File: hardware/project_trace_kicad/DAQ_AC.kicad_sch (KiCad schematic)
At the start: 1 part, among them U301 ADC3542

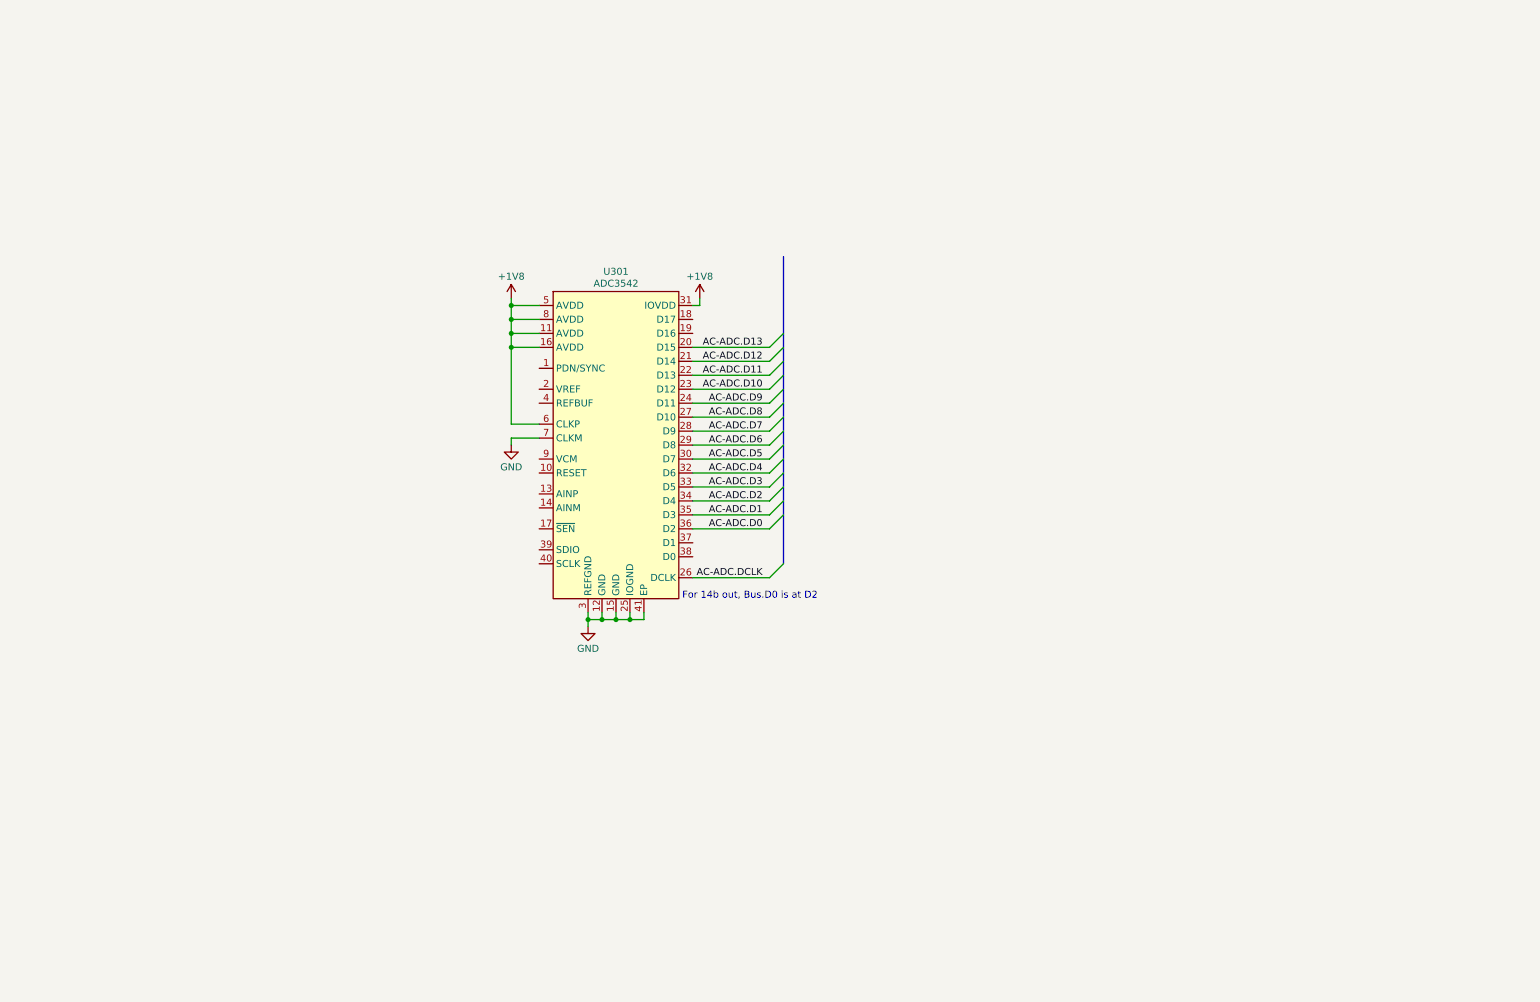
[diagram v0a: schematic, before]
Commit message: Added DAQ_AC and DAC
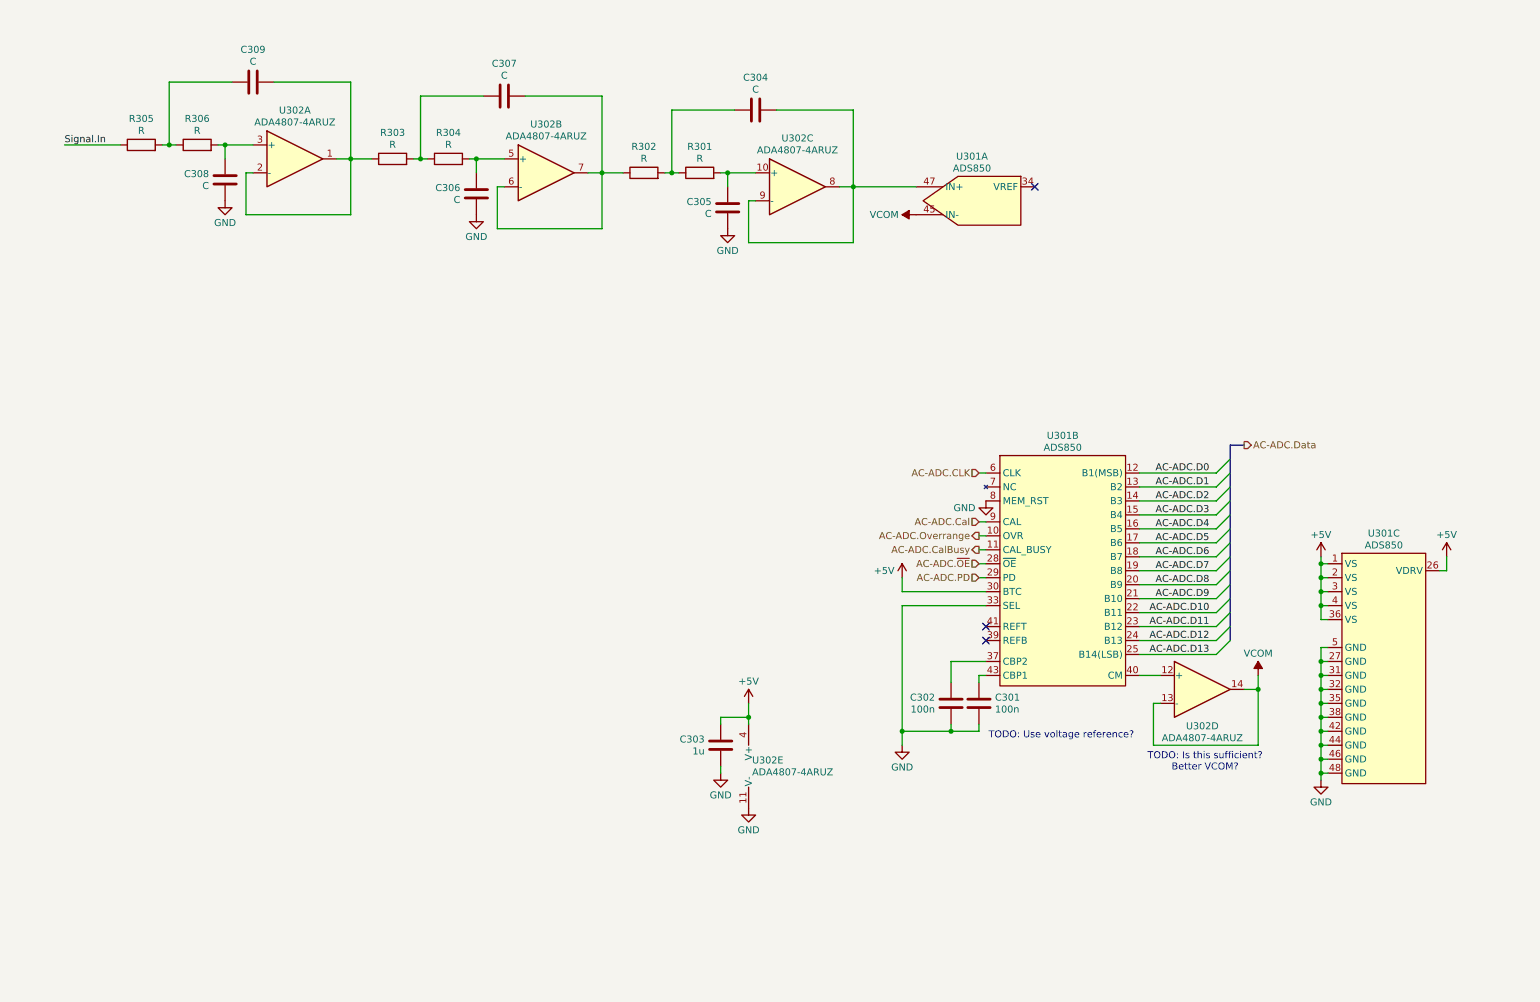
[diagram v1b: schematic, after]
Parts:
- removed U301: ADC3542, ProjectTraceFootprints:QFN-40_EP_5.1x5.1_Pitch0.4mm-RSB0040F, symbol ProjectTraceSymbols:ADC3542
- added C301, C302: 100n, symbol Device:C
- added C303: 1u, symbol Device:C
- added C304, C305, C306, C307, C308, C309: C, symbol Device:C
- added R301, R302, R303, R304, R305, R306: R, symbol Device:R
- added U301: ADS850, Package_QFP:TQFP-48_7x7mm_P0.5mm, symbol ProjectTraceSymbols:ADS850
- added U302: ADA4807-4ARUZ, Package_SO:TSSOP-14_4.4x5mm_P0.65mm, symbol Amplifier_Operational:ADA4807-4ARUZ
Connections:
- net AC-ADC.D0: now also U301.12 (B1(MSB))
- net AC-ADC.D1: now also U301.13 (B2)
- net AC-ADC.D10: now also U301.22 (B11)
- net AC-ADC.D11: now also U301.23 (B12)
- net AC-ADC.D12: now also U301.24 (B13)
- net AC-ADC.D13: now also U301.25 (B14(LSB))
- net AC-ADC.D2: now also U301.14 (B3)
- net AC-ADC.D3: now also U301.15 (B4)
- net AC-ADC.D4: now also U301.16 (B5)
- net AC-ADC.D5: now also U301.17 (B6)
- net AC-ADC.D6: now also U301.18 (B7)
- net AC-ADC.D7: now also U301.19 (B8)
- net AC-ADC.D8: now also U301.20 (B9)
- net AC-ADC.D9: now also U301.21 (B10)
- net GND: now also C301.2, C302.2, C303.1, C305.1, C306.1, C308.1, U301.27 (GND), U301.31 (GND), U301.32 (GND), U301.33 (SEL), U301.35 (GND), U301.38 (GND), U301.42 (GND), U301.44 (GND), U301.46 (GND), U301.48 (GND), U301.5 (GND), U301.8 (MEM_RST), U302.11 (V-)
- new net: C306.2, R304.2, U302.5 (+)
- new net: C307.2, R302.1, U302.6 (-), U302.7
- new net: C309.2, R303.1, U302.1, U302.2 (-)
- new net: C307.1, R303.2, R304.1
- new net: C305.2, R301.2, U302.10 (+)
- new net: C304.2, U301.47 (IN+), U302.8, U302.9 (-)
- new net: C304.1, R301.1, R302.2
- new net: C301.1, U301.43 (CBP1)
- new net: U301.40 (CM), U302.12 (+)
- new net: C302.1, U301.37 (CBP2)
- new net: C309.1, R305.2, R306.1
- new net: C308.2, R306.2, U302.3 (+)
- new net +5V: C303.2, U301.1 (VS), U301.2 (VS), U301.26 (VDRV), U301.3 (VS), U301.30 (BTC), U301.36 (VS), U301.4 (VS), U302.4 (V+)
- new net AC-ADC.CLK: U301.6 (CLK)
- new net AC-ADC.Cal: U301.9 (CAL)
- new net AC-ADC.CalBusy: U301.11 (CAL_BUSY)
- new net AC-ADC.Overrange: U301.10 (OVR)
- new net AC-ADC.PD: U301.29 (PD)
- new net AC-ADC.~{OE}: U301.28 (~{OE})
- new net Signal.In: R305.1
- new net VCOM: U301.45 (IN-), U302.13 (-), U302.14
- no-connect marks 0 -> 3
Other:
- note added: "TODO: Is this sufficient? Better VCOM?"
- note added: "TODO: Use voltage reference?"
- note removed: "For 14b out, Bus.D0 is at D2"

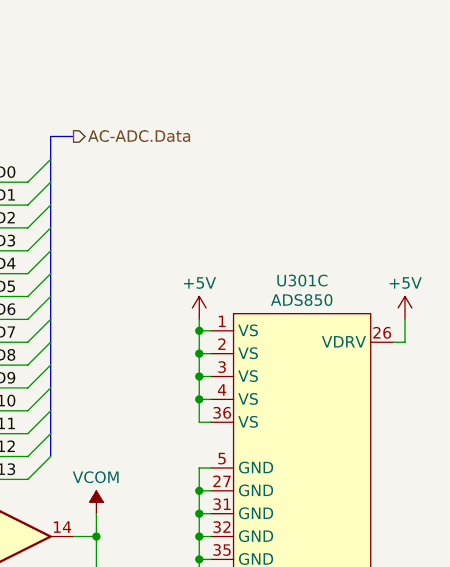
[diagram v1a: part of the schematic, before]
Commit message: Changes to DAQ-AC and Inputs
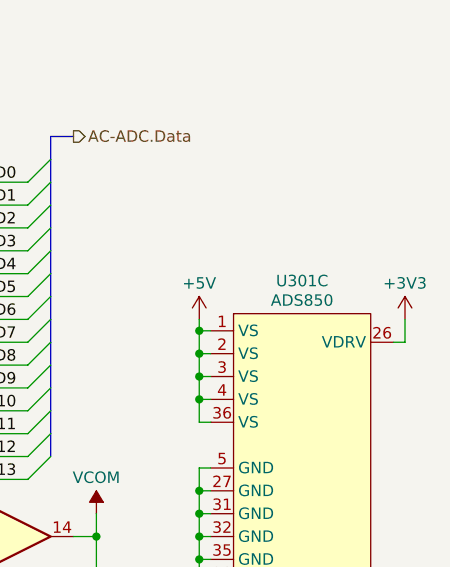
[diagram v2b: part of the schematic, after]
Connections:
- net +5V: no longer U301.26 (VDRV)
- new net +3V3: U301.26 (VDRV)
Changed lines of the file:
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@@
+	)
+	(symbol
+		(lib_id "power:+3V3")
+		(at 270.51 118.11 0)
+		(unit 1)
+		(exclude_from_sim no)
+		(in_bom yes)
+		(on_board yes)
+		(dnp no)
+		(fields_autoplaced yes)
+		(property "Reference" "#PWR0304"
+			(at 270.51 121.92 0)
+			(effects
+				(font
+					(size 1.27 1.27)
+				)
+				(hide yes)
+			)
+		)
+		(property "Value" "+3V3"
+			(at 270.51 114.1052 0)
+			(effects
+				(font
+					(size 1.27 1.27)
+				)
+			)
+		)
+		(property "Footprint" ""
+			(at 270.51 118.11 0)
+			(effects
+				(font
+					(size 1.27 1.27)
+				)
+				(hide yes)
+			)
+		)
+		(property "Datasheet" ""
+			(at 270.51 118.11 0)
+			(effects
+				(font
+					(size 1.27 1.27)
+				)
+				(hide yes)
+			)
+		)
+		(property "Description" "Power symbol creates a global label with name \"+3V3\""
+			(at 270.51 118.11 0)
+			(effects
+				(font
+					(size 1.27 1.27)
+				)
+				(hide yes)
+			)
+		)
+		(pin "1"
+		)
+		(instances
+			(project ""
+				(path "/af51f4e5-b952-4b0e-baf2-78a72fb86fcd/ac2add4a-2a5e-456c-897d-914b794115d5"
+					(reference "#PWR0304")
+					(unit 1)
+				)
+			)
+		)
 	)
 	(symbol
@@
 					(unit 1)
 				)
-			)
-		)
-	)
-	(symbol
-		(lib_id "power:+5V")
-		(at 270.51 118.11 0)
-		(unit 1)
-		(exclude_from_sim no)
-		(in_bom yes)
-		(on_board yes)
-		(dnp no)
-		(fields_autoplaced yes)
-		(property "Reference" "#PWR0304"
-			(at 270.51 121.92 0)
-			(effects
-				(font
-					(size 1.27 1.27)
-				)
-				(hide yes)
-			)
-		)
-		(property "Value" "+5V"
-			(at 270.51 114.1052 0)
-			(effects
-				(font
-					(size 1.27 1.27)
-				)
-			)
-		)
-		(property "Footprint" ""
-			(at 270.51 118.11 0)
-			(effects
-				(font
-					(size 1.27 1.27)
-				)
-				(hide yes)
-			)
-		)
-		(property "Datasheet" ""
-			(at 270.51 118.11 0)
-			(effects
-				(font
-					(size 1.27 1.27)
-				)
-				(hide yes)
-			)
-		)
-		(property "Description" "Power symbol creates a global label with name \"+5V\""
-			(at 270.51 118.11 0)
-			(effects
-				(font
-					(size 1.27 1.27)
-				)
-				(hide yes)
-			)
-		)
-		(pin "1"
-		)
-		(instances
-			(project "project_trace_kicad"
-				(path "/af51f4e5-b952-4b0e-baf2-78a72fb86fcd/ac2add4a-2a5e-456c-897d-914b794115d5"
-					(reference "#PWR0304")
-					(unit 1)
-				)

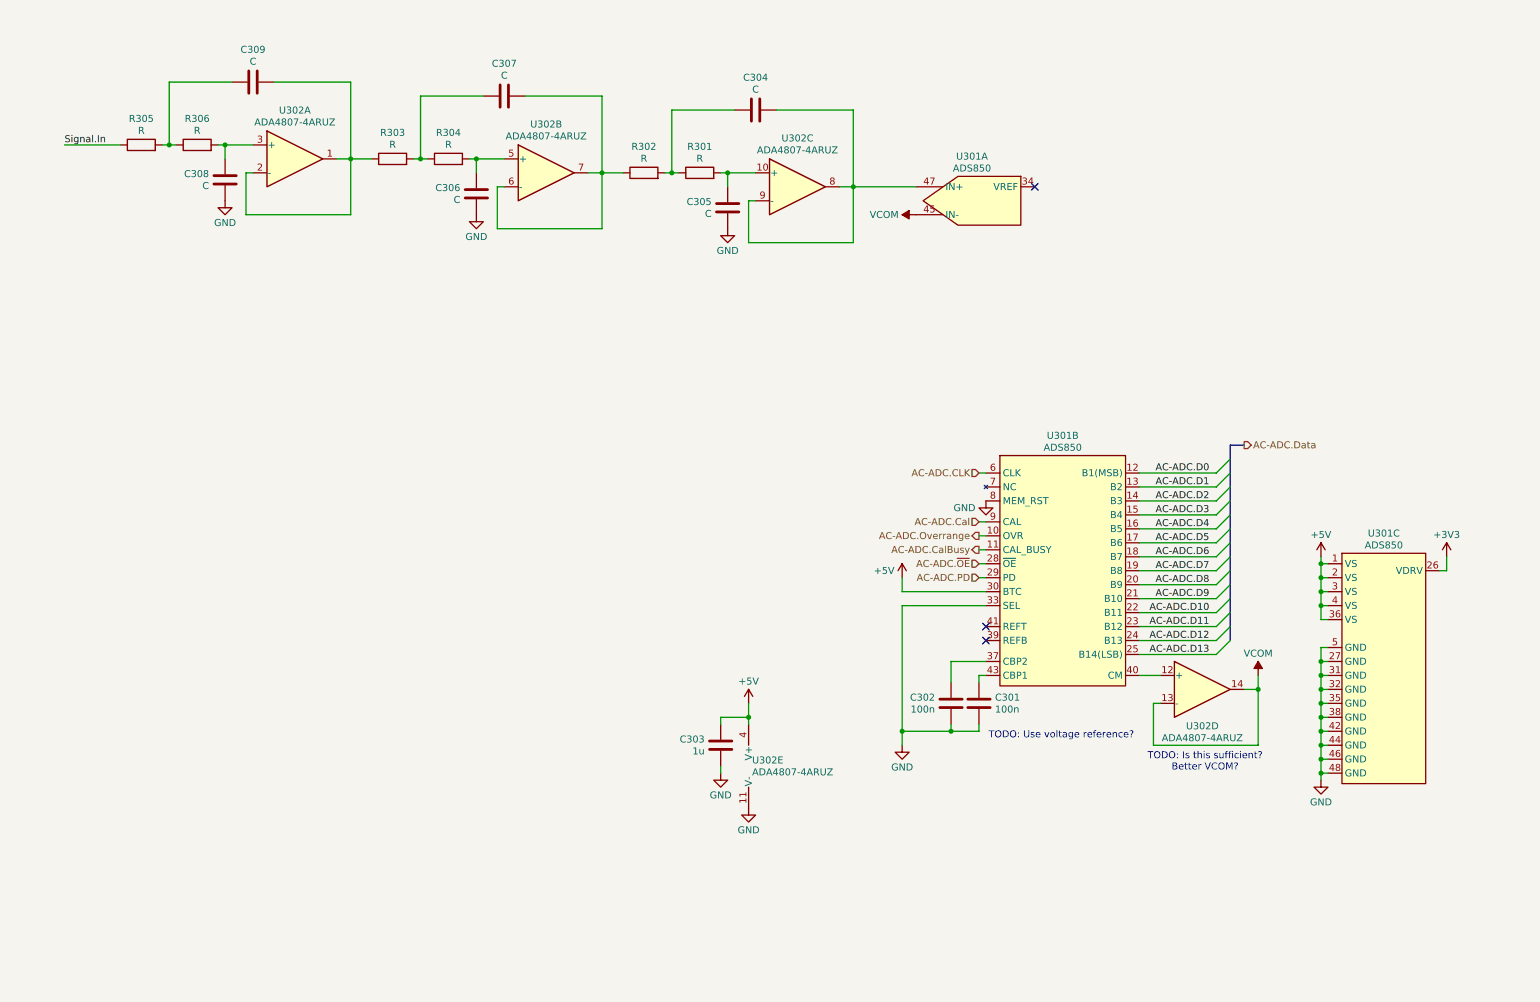
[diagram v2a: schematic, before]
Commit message: Add Decoupling, Fix Bugs
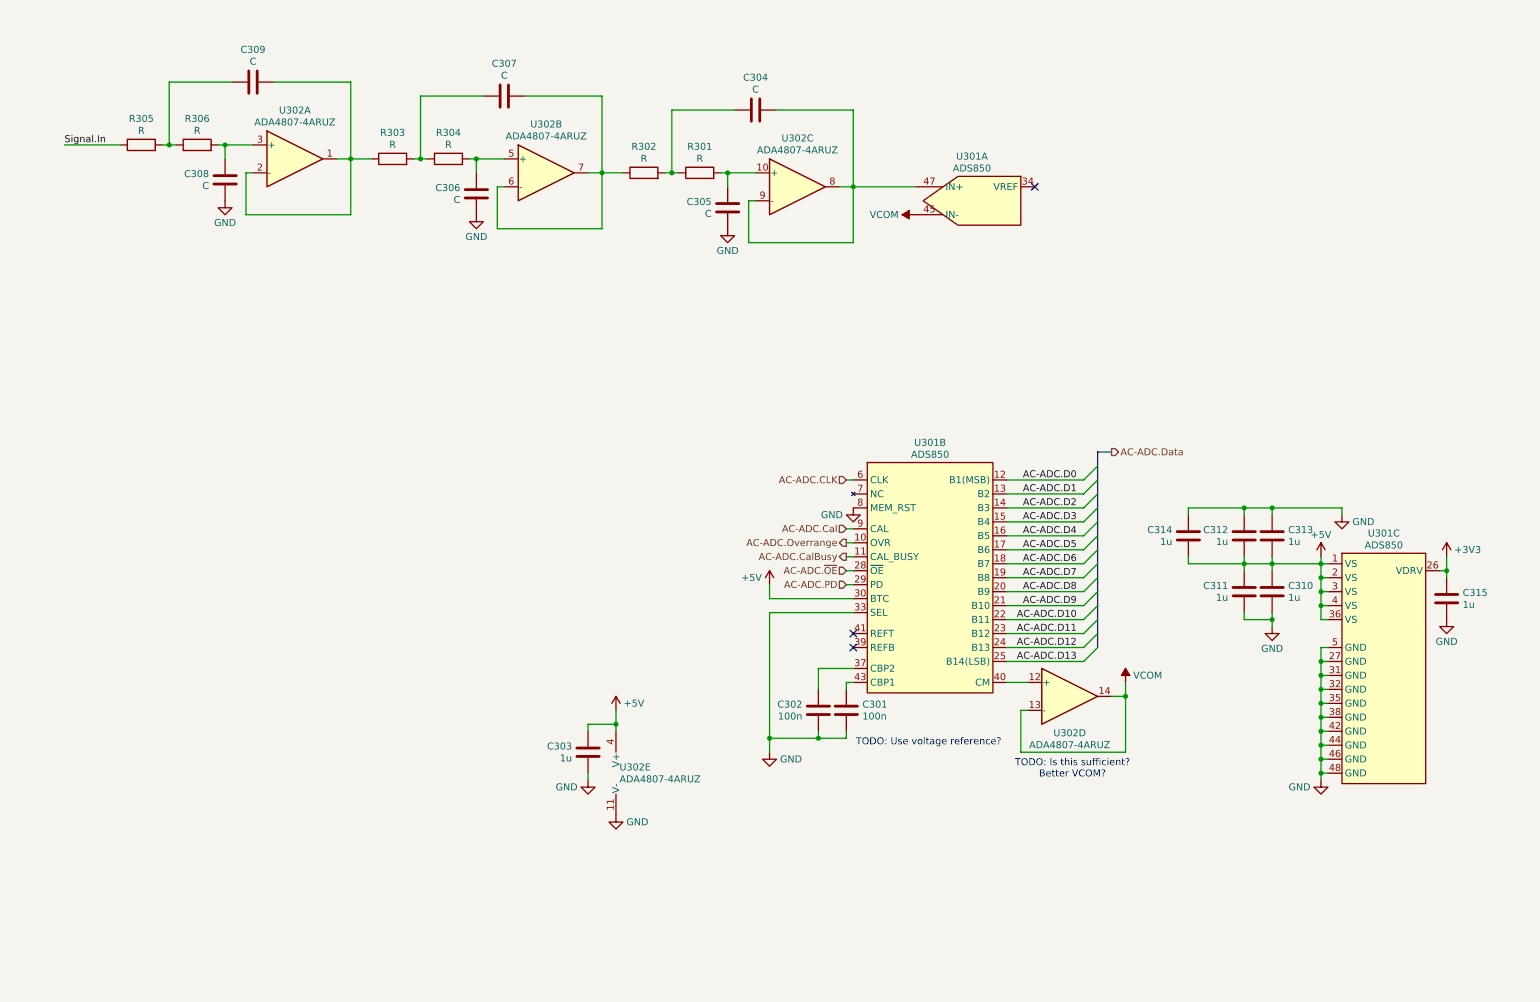
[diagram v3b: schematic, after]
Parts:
- added C310, C311, C312, C313, C314, C315: 1u, symbol Device:C
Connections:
- net +3V3: now also C315.2
- net +5V: now also C310.2, C311.2, C312.1, C313.1, C314.1
- net GND: now also C310.1, C311.1, C312.2, C313.2, C314.2, C315.1
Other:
- moved on the sheet: C301, C302, C303, U301B, U302D, U302E

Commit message: Fix Mistakes, Reduce Scope, improve Flexibility
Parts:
- U302: DigikeyPN (none) -> 505-ADA4807-4ARUZ-ND

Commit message: Before Changes to Input Section
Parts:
- removed C303, C315: 1u, symbol Device:C
- removed C308, C309: C, symbol Device:C
- removed U301: ADS850, Package_QFP:TQFP-48_7x7mm_P0.5mm, symbol ProjectTraceSymbols:ADS850
- removed U302: ADA4807-4ARUZ, Package_SO:TSSOP-14_4.4x5mm_P0.65mm, symbol Amplifier_Operational:ADA4807-4ARUZ
- added C308, C315, C319: 10u, Capacitor_SMD:C_0603_1608Metric_Pad1.08x0.95mm_HandSolder, symbol Device:C_Small
- added C309, C318, C320: 100n, Capacitor_SMD:C_0603_1608Metric_Pad1.08x0.95mm_HandSolder, symbol Device:C_Small
- added C316, C317, C321: 100n, Capacitor_SMD:C_0603_1608Metric_Pad1.08x0.95mm_HandSolder, symbol Device:C
- added R307, R308: 10k, Resistor_SMD:R_0603_1608Metric_Pad0.98x0.95mm_HandSolder, symbol Device:R
- added R309: 15k, Resistor_SMD:R_0603_1608Metric_Pad0.98x0.95mm_HandSolder, symbol Device:R
- added R310: 388R, Resistor_SMD:R_0603_1608Metric_Pad0.98x0.95mm_HandSolder, symbol Device:R
- added U301: ADS1602, symbol ProjectTraceSymbols:ADS1602
- added U303: THS4521ID, Package_SO:SOIC-8_3.9x4.9mm_P1.27mm, symbol Amplifier_Difference:THS4521ID
- added U304: LM358, Package_SO:MSOP-8_3x3mm_P0.65mm, symbol Amplifier_Operational:LM358
- C301, C302: footprint (none) -> Capacitor_SMD:C_0603_1608Metric_Pad1.08x0.95mm_HandSolder
- C304, C305: value C -> 100p; footprint (none) -> Capacitor_SMD:C_0603_1608Metric_Pad1.08x0.95mm_HandSolder; Extra (none) -> C0G
- C306, C307: value C -> 100n; footprint (none) -> Capacitor_SMD:C_0603_1608Metric_Pad1.08x0.95mm_HandSolder
- C310, C311, C312, C313, C314: value 1u -> 100n; footprint (none) -> Capacitor_SMD:C_0603_1608Metric_Pad1.08x0.95mm_HandSolder
- R301, R302: value R -> 24R9; footprint (none) -> Resistor_SMD:R_0603_1608Metric_Pad0.98x0.95mm_HandSolder; Extra (none) -> 1%
- R303, R305: value R -> 234R; footprint (none) -> Resistor_SMD:R_0603_1608Metric_Pad0.98x0.95mm_HandSolder; Extra (none) -> 0.1%
- R304: value R -> 388R; footprint (none) -> Resistor_SMD:R_0603_1608Metric_Pad0.98x0.95mm_HandSolder; Extra (none) -> 0.1%
- R306: value R -> 37k; footprint (none) -> Resistor_SMD:R_0603_1608Metric_Pad0.98x0.95mm_HandSolder
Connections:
- net +3V3: now also C301.2, C302.2, C316.2, C317.2, R307.1, U301.18 (DVDD), U301.23 (DVDD), U301.34 (DVDD), U301.37 (IOVDD)
- net +5V: now also C306.2, C321.2, U301.10 (AVDD), U301.12 (AVDD), U301.2 (AVDD), U301.42 (AVDD), U301.7 (AVDD), U303.3 (V_{S+}), U303.7 (~{PD}), U304.8 (V+)
- net GND: now also C301.1, C302.1, C304.1, C305.2, C307.1, R306.2, C308.1, C309.1, C315.2, C316.1, C317.1, C318.2, C319.2, C320.2, C321.1, R309.1, U301.1 (AGND), U301.11 (AGND), U301.19 (DGND), U301.22 (DGND), U301.3 (AGND), U301.33 (DGND), U301.36 (DGND), U301.38 (DGND), U301.39 (AGND), U301.41 (AGND), U301.6 (AGND), U301.9 (AGND), U303.6 (V_{S-}), U304.4 (V-); no longer C301.2, C302.2, C305.1
- net VCOM: now also R303.1, R308.2, U304.1, U304.2 (-)
- net at R304.2: now also R301.1, U303.5; no longer C306.2
- net at R302.1: now also R310.2, U303.4; no longer C307.2
- net at R303.2, R304.1: now also U303.8 (+); no longer C307.1
- net at R301.2: now also C304.2, U301.5 (AINP); no longer C305.2
- net at R306.1: now also U301.8 (RBIAS); no longer R305.2
- new net: R308.1, R309.2, U304.5 (+)
- new net: C315.1, C318.1, U301.46 (VMID), U304.3 (+)
- new net: C305.1, R302.2, U301.4 (AINN)
- new net: C308.2, C309.2, U301.47 (VREFP), U301.48 (VREFP)
- new net: R307.2, U301.15 (RPULLUP)
- new net: R305.2, R310.1, U303.1 (-)
- new net: C307.2, U301.43 (VCAP)
- new net: C319.1, C320.1, U301.44 (VREFN), U301.45 (VREFN)
- new net +1V5: U303.2 (V_{OCM}), U304.6 (-), U304.7
- new net CLK: U301.40 (CLK)
- new net DOUT: U301.30 (DOUT)
- new net FSO: U301.32 (FSO)
- new net Overrange: U301.21 (OTR)
- new net SCLK: U301.28 (SCLK)
- new net SYNC: U301.20 (SYNC)
- new net ~{PD}: U301.17 (~{PD})
- new net ~{REF.EN}: U301.13 (~{REF.EN})
- new net ~{RESET}: U301.20 (SYNC)
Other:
- note added: "1.8Vpp"
- note added: "TODO: Use 3V voltage reference (ADS1602)"
- note added: "TODO: Use only RBias if using External Reference"
- note added: "TODO: Verify Footprint"
- note added: "[Vgnd+0.7;VDD-0.7]"
- note removed: "TODO: Use voltage reference?"
- moved on the sheet: C310, C311, C312, C313, C314
